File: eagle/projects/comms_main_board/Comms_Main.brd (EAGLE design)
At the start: 101.6 x 95.2 mm, 195 parts, among them J1 WRL-00593, J10 MOL-SL-2-RA, J11 MOL-SL-3-RA, J12 MOL-SL-3-RA, J13 MOL-SL-3-RA, J14 MOL-SL-3-RA, J15 MOL-SL-2-RA, J16 MOL-MINIJR-2P-RA, J17 MOL-MINIJR-2P-RA, J18 MOL-MINIJR-2P-RA, J19 MOL-MINIJR-2P-RA, J2 PRT-12639, J20 MOL-SL-2-RA, J21 RECEPTACLE-2x2-254MM, J22 MOL-SL-2-RA, J3 PRT-12639, J4 PRT-12639, J5 PRT-12639, J6 MOL-SL-3-RA, J7 MOL-SL-5-RA, J8 RECEPTACLE-2x20-254MM, J9 MOL-SL-3-RA, Q1 CSD17579Q3A, U1 TPS562209DDCT, U10 MCP4541-103E/MS, U11 TPS562209DDCT, U12 MMBT3904-HF, U13 MAX3232CSE+, U14 MAX4311, U15 MAX6371, U16 2N7002P,215, U2 LP2985-33DBVR, U3 LP5900TLX-3.3/NOPB, U4 TPS562209DDCT, U5 NDT2955, U6 LM3488MMX/NOPB, U7 PCT2075D,118, U8 MS560702BA03-50, U9 MAX-M8Q

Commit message: Begin layout
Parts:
- moved R27 37.5 mm to (84.8, 33.7)
- moved R24 36.6 mm to (85.4, 29.2), turned to 90 degrees
- moved R21 17.7 mm to (82.9, 51.4), turned to 90 degrees
- moved L6 17.1 mm to (70.0, 26.0)
- moved R23 16.8 mm to (85.1, 51.4), turned to 90 degrees
- moved C32 16.6 mm to (86.3, 78.3), turned to 270 degrees
- moved C31 16.4 mm to (71.1, 84.5), turned to 90 degrees
- moved C30 14.4 mm to (71.1, 80.5), turned to 90 degrees
- moved U12 11.6 mm to (80.7, 59.6)
- moved C24 11.2 mm to (69.1, 30.9)
- moved C14 11.0 mm to (51.9, 33.3)
- moved U11 10.9 mm to (69.3, 34.7)
- moved C34 10.8 mm to (74.7, 80.6)
- moved C33 7.89 mm to (74.8, 86.2)
- moved C12 7.66 mm to (57.6, 34.3)
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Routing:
- net RX_OUT_R: track 0.00 -> 16.1 mm
- net TX_IN_R: track 0.00 -> 11.0 mm
- net TX_OUT_R: track 0.00 -> 10.8 mm
- net RS232_C1-: track 0.00 -> 7.61 mm
- net RS232_C2-: track 0.00 -> 7.56 mm
- net RS232_C1+: track 0.00 -> 7.45 mm
- net RS232_C2+: track 0.00 -> 7.26 mm
- net RX_OUT_T: track 0.00 -> 7.26 mm
- net RX_IN_T: track 0.00 -> 6.11 mm
- net RS232_V-: track 0.00 -> 2.96 mm
- net RS232_V+: track 0.00 -> 2.58 mm
- net 3P3V_RS232: track 0.00 -> 2.50 mm

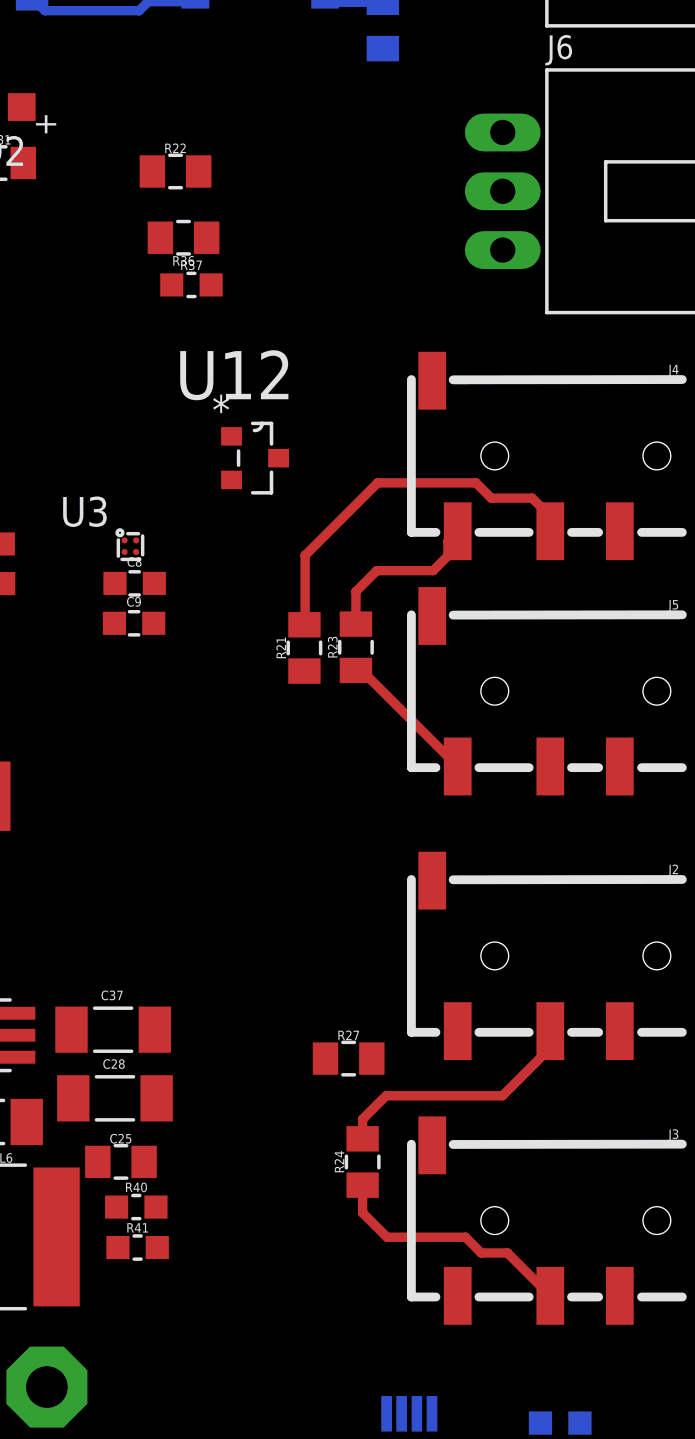
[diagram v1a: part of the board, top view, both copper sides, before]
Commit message: Layout of audio cables
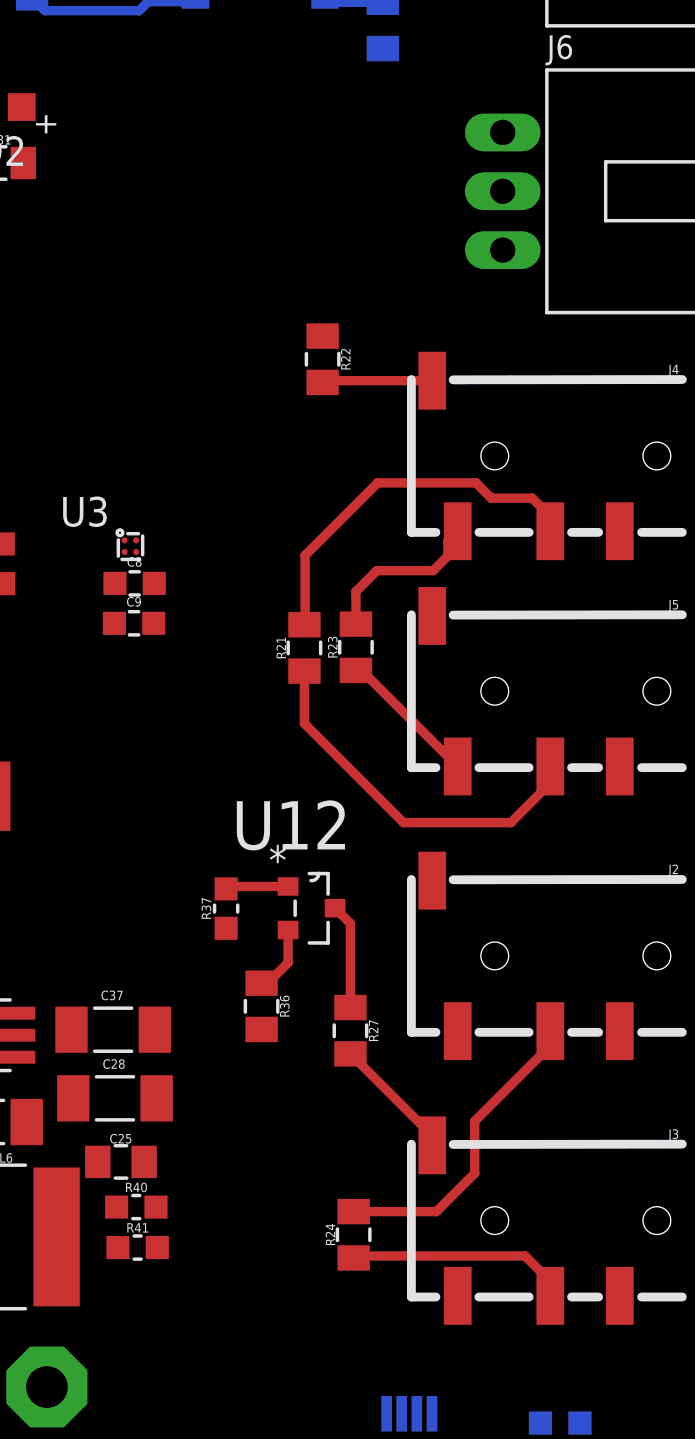
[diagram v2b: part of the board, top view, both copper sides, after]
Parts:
- moved R36 33.4 mm to (81.0, 35.9), turned to 270 degrees
- moved R37 27.0 mm to (79.5, 40.1), turned to 90 degrees
- moved U12 19.6 mm to (83.2, 40.2)
- moved R22 10.3 mm to (83.7, 63.9), turned to 270 degrees
- moved R24 3.17 mm to (85.0, 26.1)
- moved R27 1.21 mm to (84.9, 34.9), turned to 270 degrees
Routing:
- net RX_IN_R: track 0.00 -> 16.1 mm
- net TX_OUT_S: track 0.00 -> 5.41 mm
- net RX_OUT_S: track 0.00 -> 4.76 mm
- net PTT: track 0.00 -> 4.56 mm
- net PTT_BJT_E: track 0.00 -> 2.93 mm
- net PTT_BJT_B: track 0.00 -> 2.72 mm
- net TX_IN_R: track 11.0 -> 13.4 mm
- net TX_OUT_R: track 10.8 -> 9.61 mm

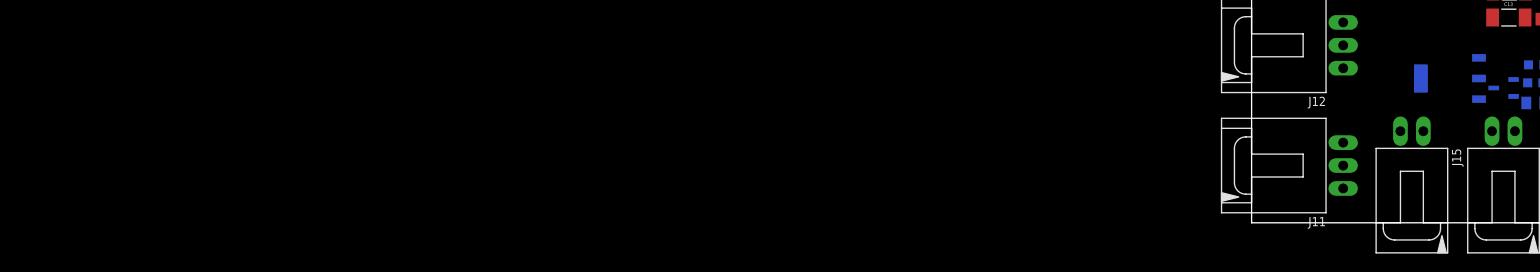
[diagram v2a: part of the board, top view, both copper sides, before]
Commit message: Fixed pin connection error in the PMOS
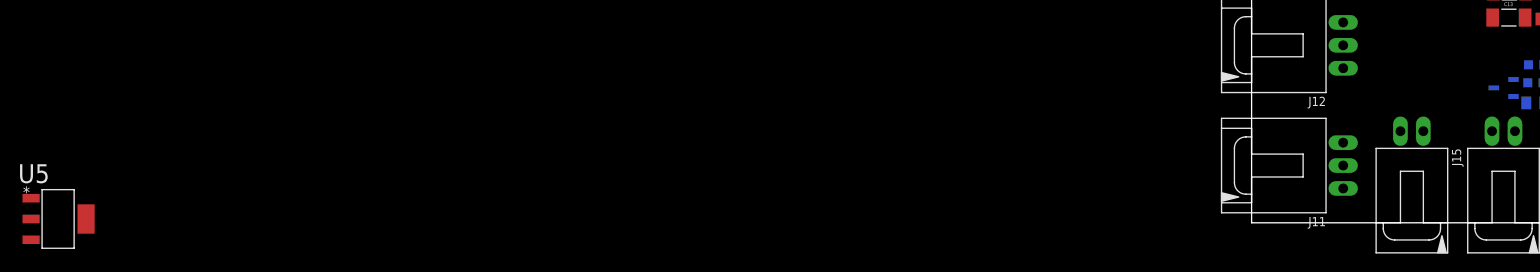
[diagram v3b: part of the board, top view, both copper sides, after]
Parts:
- moved U5 155.2 mm to (-132.4, 0.43), flipped to the top
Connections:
- net 12V_BOARD: now also U5.3; no longer U5.4
- net 12V_PI_CONTROLLED: now also U5.4; no longer U5.3
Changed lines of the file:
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@@
 <attribute name="VENDOR_PN" value="P10.0KHCT-ND" x="31.563996875" y="17.52249375" size="1.778" layer="28" rot="MR0" display="off"/>
-</element>
-<element name="U5" library="comms" package="SOT230P700X180-4N" value="NDT2955" x="22.000059375" y="16.006659375" rot="MR0">
-<attribute name="OC_NEWARK" value="58K8748" x="22.000059375" y="16.006659375" size="1.778" layer="28" rot="MR0" display="off"/>
-<attribute name="SUPPLIER" value="Fairchild" x="22.000059375" y="16.006659375" size="1.778" layer="28" rot="MR0" display="off"/>
-<attribute name="OC_FARNELL" value="1263454" x="22.000059375" y="16.006659375" size="1.778" layer="28" rot="MR0" display="off"/>
-<attribute name="MPN" value="BCP52" x="22.000059375" y="16.006659375" size="1.778" layer="28" rot="MR0" display="off"/>
-<attribute name="PACKAGE" value="SOT-223-4" x="22.000059375" y="16.006659375" size="1.778" layer="28" rot="MR0" display="off"/>
 </element>
 <element name="U16" library="comms" package="SOT95P230X110-3N" value="2N7002P,215" x="27.960040625" y="14.95311875" rot="MR0">
@@
 <attribute name="MANUFACTURER_PN" value="ERJ-6GEY0R00V" x="31.463203125" y="13.299940625" size="1.778" layer="28" rot="MR0" display="off"/>
 <attribute name="VENDOR_PN" value="P0.0ACT-ND" x="31.463203125" y="13.299940625" size="1.778" layer="28" rot="MR0" display="off"/>
+</element>
+<element name="U5" library="comms" package="SOT230P700X180-4N" value="NDT2955" x="-132.375821875" y="0.4259625">
+<attribute name="VENDOR_PN" value="NDT2955CT-ND" x="-132.375821875" y="0.4259625" size="1.778" layer="27" display="off"/>
+<attribute name="VENDOR" value="Digi-Key" x="-132.375821875" y="0.4259625" size="1.778" layer="27" display="off"/>
+<attribute name="MANUFACTURER" value="Fairchild" x="-132.375821875" y="0.4259625" size="1.778" layer="27" display="off"/>
+<attribute name="MANUFACTURER_PN" value="NDT2955" x="-132.375821875" y="0.4259625" size="1.778" layer="27" display="off"/>
+<attribute name="PACKAGE" value="SOT-223-4" x="-132.375821875" y="0.4259625" size="1.778" layer="27" display="off"/>
 </element>
 </elements>
@@
 <contactref element="R10" pad="2"/>
 <contactref element="R8" pad="2"/>
-<contactref element="U5" pad="4"/>
-<wire x1="65.582725" y1="55.370571875" x2="69.892540625" y2="54.175978125" width="0" layer="19" extent="1-1"/>
-<wire x1="55.43383125" y1="59.4553" x2="65.582725" y2="55.370571875" width="0" layer="19" extent="1-1"/>
+<contactref element="U5" pad="3"/>
+<wire x1="-24.13" y1="114.3" x2="-135.375821875" y2="-1.8740375" width="0" layer="19" extent="1-1"/>
+<wire x1="55.43383125" y1="59.4553" x2="-24.13" y2="114.3" width="0" layer="19" extent="1-1"/>
+<wire x1="65.582725" y1="55.370571875" x2="55.43383125" y2="59.4553" width="0" layer="19" extent="1-1"/>
+<wire x1="69.892540625" y1="54.175978125" x2="65.582725" y2="55.370571875" width="0" layer="19" extent="1-1"/>
 <wire x1="71.755" y1="13.97" x2="69.892540625" y2="54.175978125" width="0" layer="19" extent="1-1"/>
 <wire x1="30.713996875" y1="17.52249375" x2="71.755" y2="13.97" width="0" layer="19" extent="16-16"/>
 <wire x1="30.463203125" y1="13.299940625" x2="30.713996875" y2="17.52249375" width="0" layer="19" extent="16-16"/>
-<wire x1="18.774259375" y1="16.006659375" x2="30.463203125" y2="13.299940625" width="0" layer="19" extent="16-16"/>
-<wire x1="-24.13" y1="114.3" x2="55.43383125" y2="59.4553" width="0" layer="19" extent="1-1"/>
 </signal>
 <signal name="DCDC_STEPUP_ISENSE_RES">
@@
 <contactref element="J20" pad="1"/>
 <contactref element="R10" pad="1"/>
-<contactref element="U5" pad="3"/>
 <contactref element="U5" pad="2"/>
-<wire x1="32.463203125" y1="13.299940625" x2="39.37" y2="10.16" width="0" layer="19" extent="16-16"/>
-<wire x1="25.225859375" y1="13.720659375" x2="32.463203125" y2="13.299940625" width="0" layer="19" extent="16-16"/>
-<wire x1="25.225859375" y1="16.006659375" x2="25.225859375" y2="13.720659375" width="0" layer="19" extent="16-16"/>
+<contactref element="U5" pad="4"/>
+<wire x1="-129.275821875" y1="0.4259625" x2="-135.375821875" y2="0.4259625" width="0" layer="19" extent="1-1"/>
+<wire x1="32.463203125" y1="13.299940625" x2="-129.275821875" y2="0.4259625" width="0" layer="19" extent="1-16"/>
+<wire x1="39.37" y1="10.16" x2="32.463203125" y2="13.299940625" width="0" layer="19" extent="16-16"/>
 </signal>
 <signal name="12V_PMOS_G">
@@
 <contactref element="U16" pad="3"/>
 <contactref element="U5" pad="1"/>
-<wire x1="26.867840625" y1="14.95311875" x2="32.413996875" y2="17.52249375" width="0" layer="19" extent="16-16"/>
-<wire x1="25.225859375" y1="18.292659375" x2="26.867840625" y2="14.95311875" width="0" layer="19" extent="16-16"/>
+<wire x1="26.867840625" y1="14.95311875" x2="-135.375821875" y2="2.7259625" width="0" layer="19" extent="1-16"/>
+<wire x1="32.413996875" y1="17.52249375" x2="26.867840625" y2="14.95311875" width="0" layer="19" extent="16-16"/>
 </signal>
 </signals>
